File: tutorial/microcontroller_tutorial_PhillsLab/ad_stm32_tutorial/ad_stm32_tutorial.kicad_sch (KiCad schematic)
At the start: 0 parts

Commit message: VIDEO #3 :: finished schematic
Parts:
- added C1, C2: 4u7, Capacitor_SMD:C_0805_2012Metric, symbol Device:C
- added C3: 22p, Capacitor_SMD:C_0603_1608Metric, symbol Device:C
- added L1: NRH2412T100MNGH, Inductor_SMD:NRH2412T2R2MNGH, symbol Device:NRH2412T100MNGH
- added R1, R2: 887k, Resistor_SMD:R_0603_1608Metric, symbol Device:R
- added U1: ~, Package_TO_SOT_SMD:SOT-23-6, symbol Regulator_Switching:LTC3405
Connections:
- new net: C3.1, R1.1, R2.1, U1.5 (VFB)
- new net: L1.1, U1.3 (SW)
- new net +3V3: C2.1, C3.2, L1.2, R1.2
- new net +5V: C1.1, U1.1 (RUN), U1.4 (VIN)
- new net GND: C1.2, C2.2, R2.2, U1.2 (GND), U1.6 (MODE)

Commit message: VIDEO #3 :: Added USB-C connector
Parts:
- added C4, C5: 100n, Capacitor_SMD:C_0603_1608Metric, symbol Device:C
- added FB1: 120R, Inductor_SMD:L_6.3x6.3_H3, symbol Device:FerriteBead
- added J1: USB_C_Receptacle_USB2.0_16P, Connector_USB:USB_C_Receptacle_GCT_USB4105-xx-A_16P_TopMnt_Horizontal, symbol Connector:USB_C_Receptacle_USB2.0_16P
- added R3, R4: 5k1, Resistor_SMD:R_0603_1608Metric, symbol Device:R
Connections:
- net +5V: now also C5.1, FB1.2
- net GND: now also C4.2, C5.2, J1.A1 (GND), J1.A12 (GND), J1.B1 (GND), J1.B12 (GND), R3.2, R4.2
- net BUCK_VFB: now reaches C3.1, R1.1, R2.1, U1.5 (VFB)
- net BUCK_SW: now reaches L1.1, U1.3 (SW)
- new net USB_CC1: J1.A5 (CC1), R4.1
- new net USB_CC2: J1.B5 (CC2), R3.1
- new net USB_D_N: J1.A7 (D-), J1.B7 (D-)
- new net USB_D_P: J1.A6 (D+), J1.B6 (D+)
- new net VBUS: C4.1, FB1.1, J1.A4 (VBUS), J1.A9 (VBUS), J1.B4 (VBUS), J1.B9 (VBUS)
- no-connect marks 0 -> 3
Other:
- moved on the sheet: C1, C2, C3, L1, R1, R2, U1

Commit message: Finished Video 4 of Phil's Lab Microcontroller-Based Hardware Design tutorial
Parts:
- added C10, C6, C7, C8, C9: 100n, Capacitor_SMD:C_0603_1608Metric, symbol Device:C
- added C11, C12: 10p, Capacitor_SMD:C_0603_1608Metric, symbol Device:C
- added FB2: 120R, Inductor_SMD:L_6.3x6.3_H3, symbol Device:FerriteBead
- added J2: TagConnect_TC2030-NL, Connector:Tag-Connect_TC2030-IDC-NL_2x03_P1.27mm_Vertical, symbol Connector:Conn_ARM_SWD_TagConnect_TC2030-NL
- added R5: 5k1, Resistor_SMD:R_0603_1608Metric, symbol Device:R
- added U2: STM32F042G6Ux, Package_DFN_QFN:QFN-28_4x4mm_P0.5mm, symbol MCU_ST_STM32F0:STM32F042G6Ux
- added Y2: Crystal_GND24, symbol Device:Crystal_GND24
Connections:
- net +3V3: now also C6.2, C7.2, C8.1, FB2.1, J2.1 (VCC), U2.17 (VDD), U2.18 (VDDIO2)
- net GND: now also C10.2, C11.1, C11.2, C12.2, C6.1, C7.1, C8.2, C9.2, J2.5 (GND), R5.2, U2.16 (VSSA), U2.2 (PF0), Y2.1, Y2.2, Y2.4
- net USB_D_N: now also U2.19 (PA9/PA11)
- net USB_D_P: now also U2.20 (PA10/PA12)
- new net +3V3A: C9.1, FB2.2, U2.5 (VDDA)
- new net BOOT0: R5.1, U2.1 (PB8)
- new net NRST: C10.1, J2.3 (~{RESET}), U2.4 (NRST)
- new net OSC_OUT: C12.1, U2.3 (PF1), Y2.3
- new net SWCLK: J2.4 (SWCLK), U2.22 (PA14)
- new net SWDIO: J2.2 (SWDIO), U2.21 (PA13)
- no-connect marks 3 -> 4

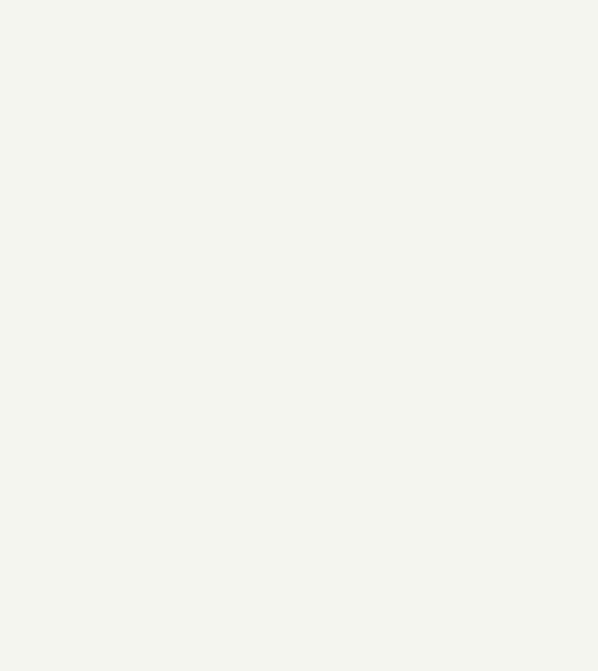
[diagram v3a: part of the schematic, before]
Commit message: Phil's lab Microcontroller tutorial - Started adding sensor
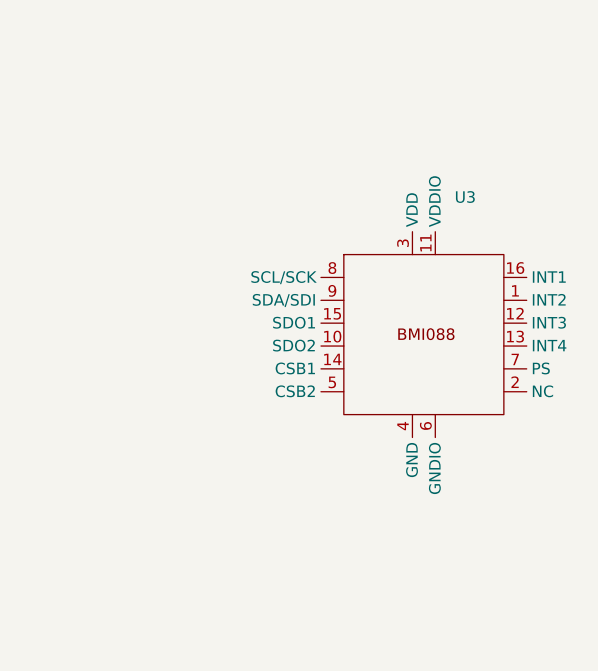
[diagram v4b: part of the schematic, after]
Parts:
- added U3: ~, symbol Sensor_Motion:BMI088
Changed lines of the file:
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@@
+	)
+	(symbol
+		(lib_id "Sensor_Motion:BMI088")
+		(at 214.63 110.49 0)
+		(unit 1)
+		(exclude_from_sim no)
+		(in_bom yes)
+		(on_board yes)
+		(dnp no)
+		(fields_autoplaced yes)
+		(property "Reference" "U3"
+			(at 218.0433 95.25 0)
+			(effects
+				(font
+					(size 1.27 1.27)
+				)
+				(justify left)
+			)
+		)
+		(property "Value" "~"
+			(at 218.0433 96.52 0)
+			(effects
+				(font
+					(size 1.27 1.27)
+				)
+				(justify left)
+			)
+		)
+		(property "Footprint" ""
+			(at 214.63 110.49 0)
+			(effects
+				(font
+					(size 1.27 1.27)
+				)
+				(hide yes)
+			)
+		)
+		(property "Datasheet" ""
+			(at 214.63 110.49 0)
+			(effects
+				(font
+					(size 1.27 1.27)
+				)
+				(hide yes)
+			)
+		)
+		(property "Description" ""
+			(at 214.63 110.49 0)
+			(effects
+				(font
+					(size 1.27 1.27)
+				)
+				(hide yes)
+			)
+		)
+		(pin "5"
+		)
+		(pin "2"
+		)
+		(pin "12"
+		)
+		(pin "7"
+		)
+		(pin "13"
+		)
+		(pin "4"
+		)
+		(pin "16"
+		)
+		(pin "3"
+		)
+		(pin "8"
+		)
+		(pin "14"
+		)
+		(pin "10"
+		)
+		(pin "15"
+		)
+		(pin "9"
+		)
+		(pin "6"
+		)
+		(pin "1"
+		)
+		(pin "11"
+		)
+		(instances
+			(project ""
+				(path "/1de9bebc-63cb-48a8-9c76-8c1d08f0b3c6"
+					(reference "U3")
+					(unit 1)
+				)
+			)
+		)
 	)
 	(symbol

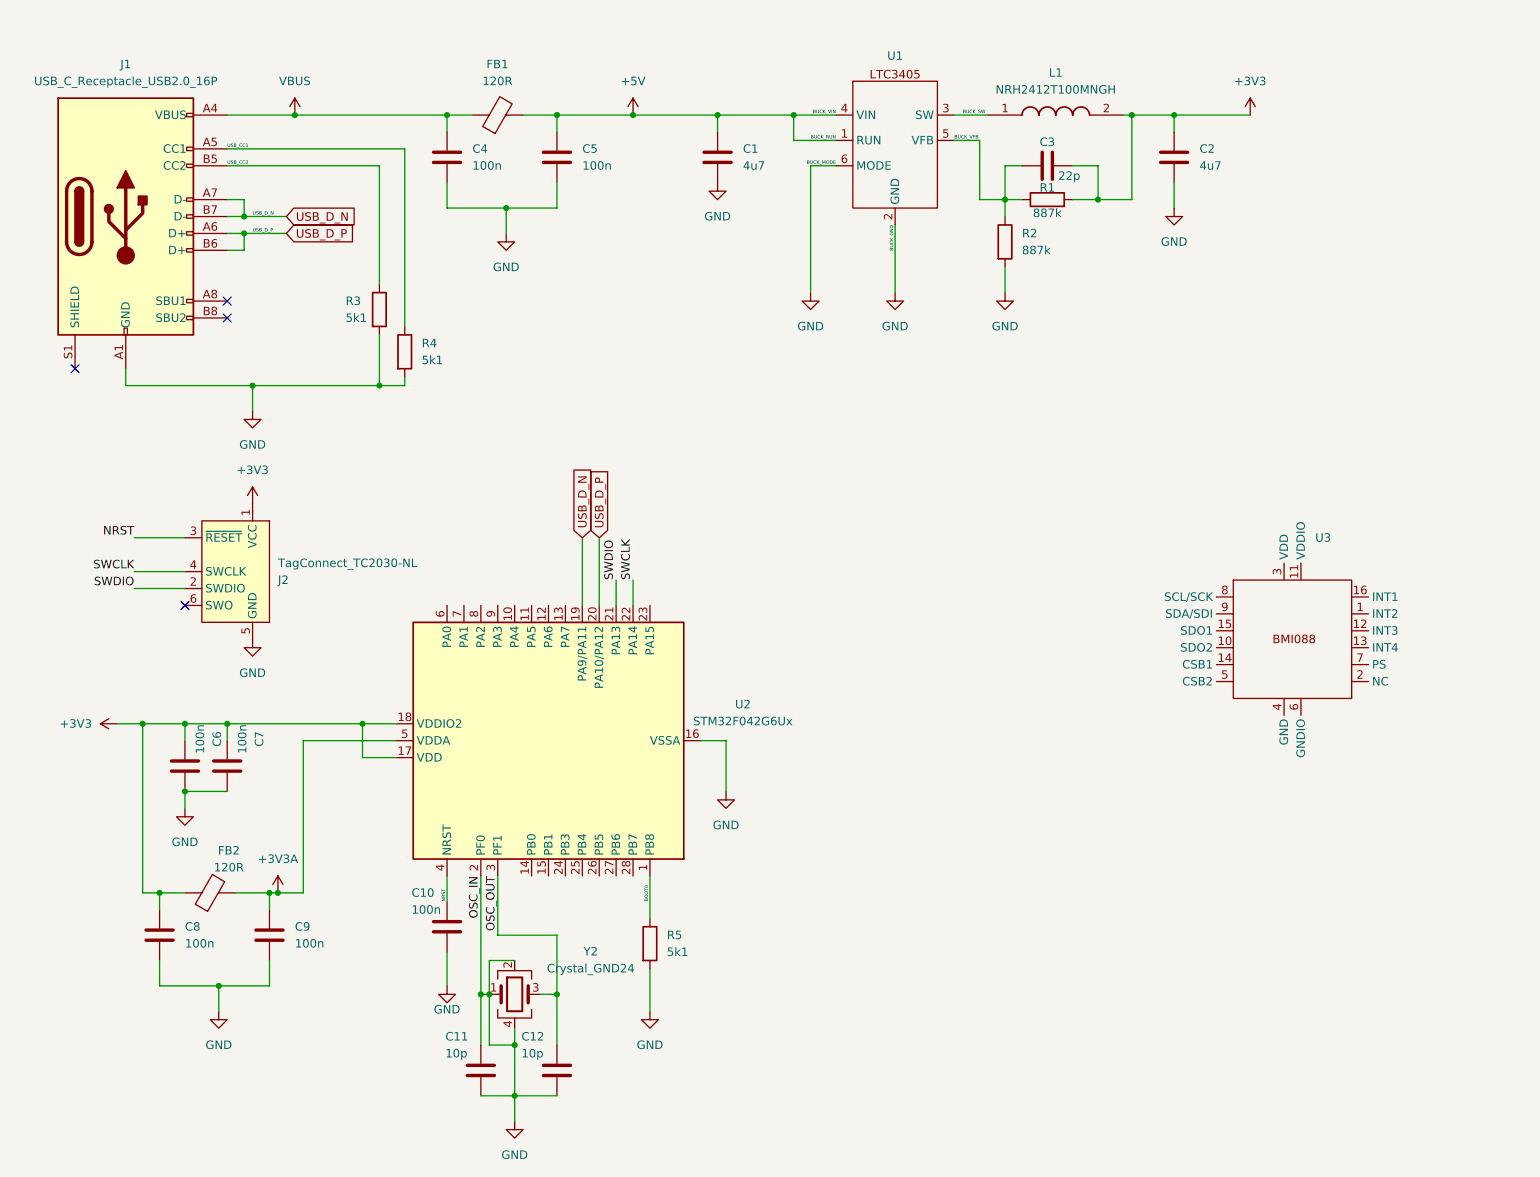
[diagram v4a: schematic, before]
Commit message: Adding BMI088 to project
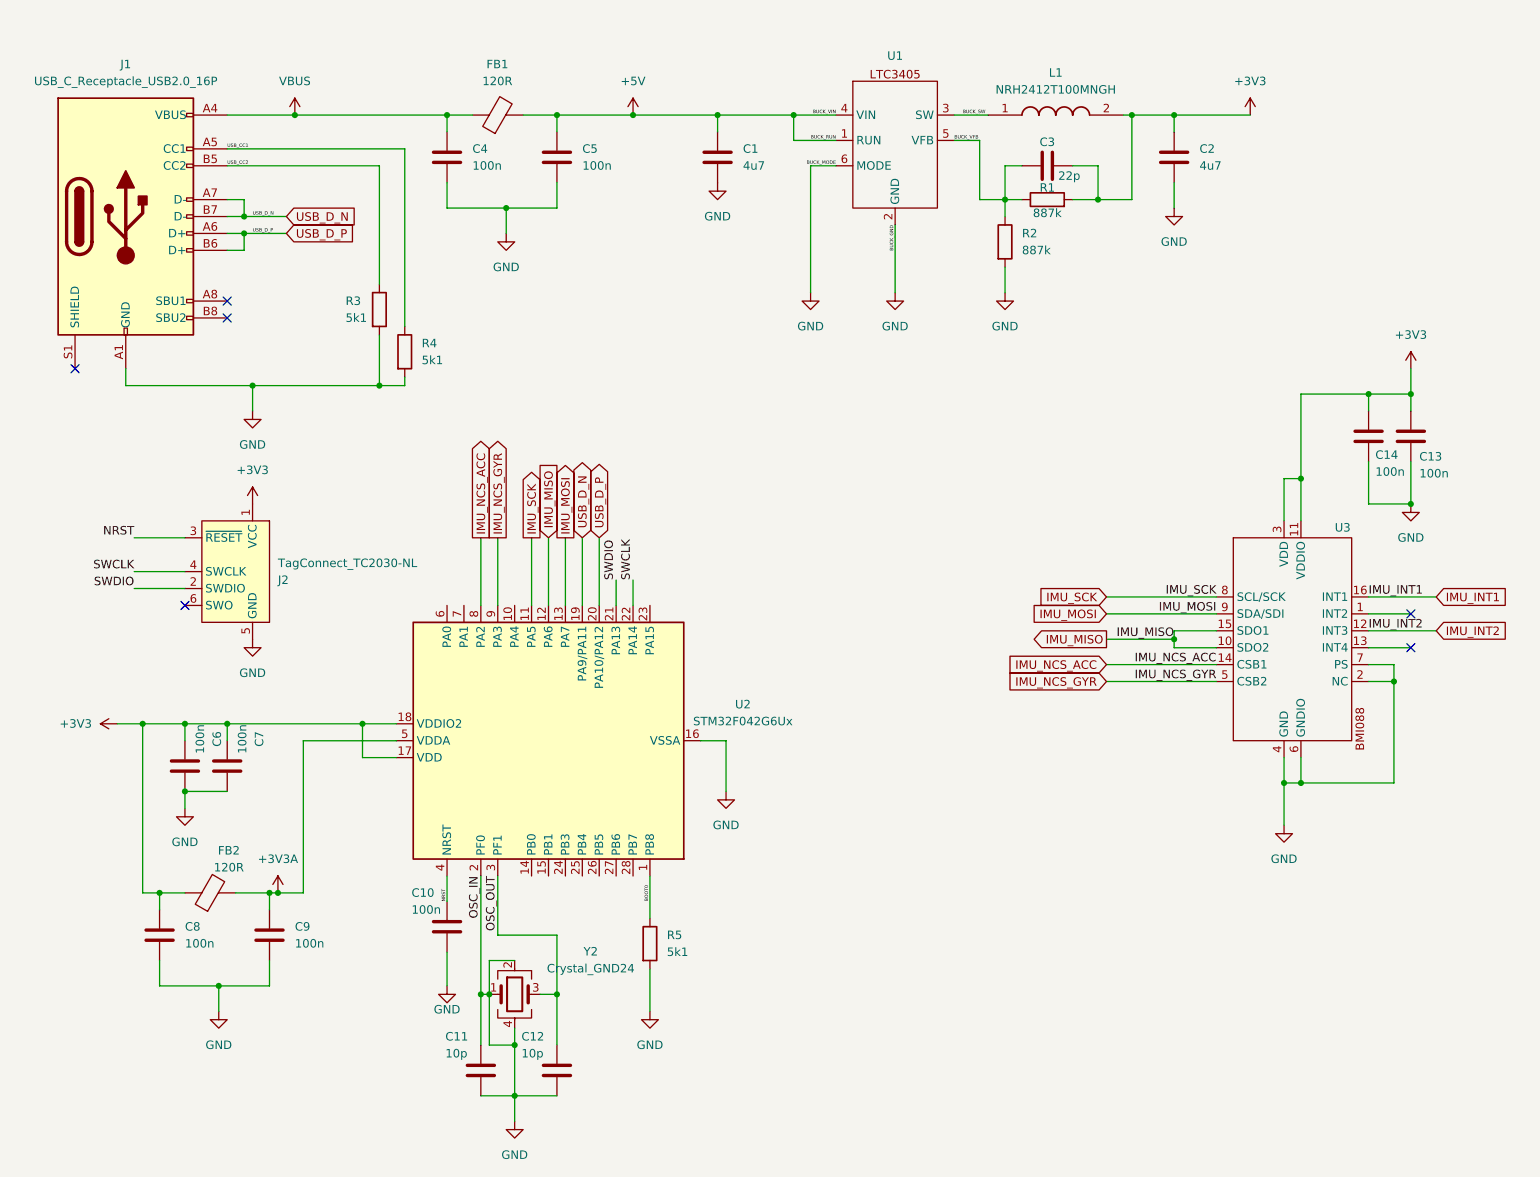
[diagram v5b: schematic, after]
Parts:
- added C13, C14: 100n, Capacitor_SMD:C_0603_1608Metric, symbol Device:C
- U3: footprint (none) -> Package_LGA:LGA-16_4.5x3mm_P0.5mm
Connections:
- net +3V3: now also U3.11 (VDDIO), U3.3 (VDD), C13.1, C14.1
- net GND: now also U3.2 (NC), U3.4 (GND), U3.6 (GNDIO), U3.7 (PS), C13.2, C14.2
- net IMU_MISO: now reaches U3.10 (SDO2)
- net IMU_MISO: now also U2.12 (PA6), U3.15 (SDO1)
- net IMU_INT2: now reaches U3.12 (INT3)
- net IMU_NCS_ACC: now reaches U3.14 (CSB1)
- net IMU_NCS_ACC: now also U2.8 (PA2)
- net IMU_INT1: now reaches U3.16 (INT1)
- net IMU_NCS_GYR: now reaches U3.5 (CSB2)
- net IMU_NCS_GYR: now also U2.9 (PA3)
- net IMU_SCK: now reaches U3.8 (SCL/SCK)
- net IMU_SCK: now also U2.11 (PA5)
- net IMU_MOSI: now reaches U3.9 (SDA/SDI)
- net IMU_MOSI: now also U2.13 (PA7)
- no-connect marks 4 -> 6
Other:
- moved on the sheet: U3

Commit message: Finished schematic
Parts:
- added J3: Conn_01x06, symbol Connector_Generic:Conn_01x06
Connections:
- net +3V3: now also J3.1 (Pin_1)
- net GND: now also J3.2 (Pin_2), J3.4 (Pin_4), J3.6 (Pin_6)
- net I2C_SCL: now reaches U2.27 (PB6)
- net I2C_SCL: now also J3.3 (Pin_3)
- net I2C_SDA: now reaches U2.28 (PB7)
- net I2C_SDA: now also J3.5 (Pin_5)
- no-connect marks 6 -> 15
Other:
- moved on the sheet: R5

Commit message: Updated schematic
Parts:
- J3: footprint (none) -> Connector_Phoenix_MC:PhoenixContact_MC_1,5_6-GF-3.81_1x06_P3.81mm_Horizontal_ThreadedFlange
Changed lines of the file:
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@@
 			)
 		)
-		(property "Footprint" ""
+		(property "Footprint" "Connector_Phoenix_MC:PhoenixContact_MC_1,5_6-GF-3.81_1x06_P3.81mm_Horizontal_ThreadedFlange"
 			(at 162.56 157.48 0)
 			(effects

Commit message: Changed few footprints for stm32 project
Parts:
- J3: footprint Connector_Phoenix_MC:PhoenixContact_MC_1,5_6-GF-3.81_1x06_P3.81mm_Horizontal_ThreadedFlange -> Connector_JST:JST_XH_S6B-XH-A_1x06_P2.50mm_Horizontal
- Y2: footprint (none) -> Crystal:Crystal_SMD_TXC_7M-4Pin_3.2x2.5mm
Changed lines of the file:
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@@
 			)
 		)
-		(property "Footprint" ""
+		(property "Footprint" "Crystal:Crystal_SMD_TXC_7M-4Pin_3.2x2.5mm"
 			(at 97.79 163.83 0)
 			(effects
@@
 			)
 		)
-		(property "Footprint" "Connector_Phoenix_MC:PhoenixContact_MC_1,5_6-GF-3.81_1x06_P3.81mm_Horizontal_ThreadedFlange"
+		(property "Footprint" "Connector_JST:JST_XH_S6B-XH-A_1x06_P2.50mm_Horizontal"
 			(at 162.56 157.48 0)
 			(effects
